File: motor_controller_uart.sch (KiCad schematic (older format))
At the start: 42 parts, among them J10 DB9_Male, J11 DB9_Male, J8 DB9_Male, J9 DB9_Male, U2 MAX3232, U4 MAX3232

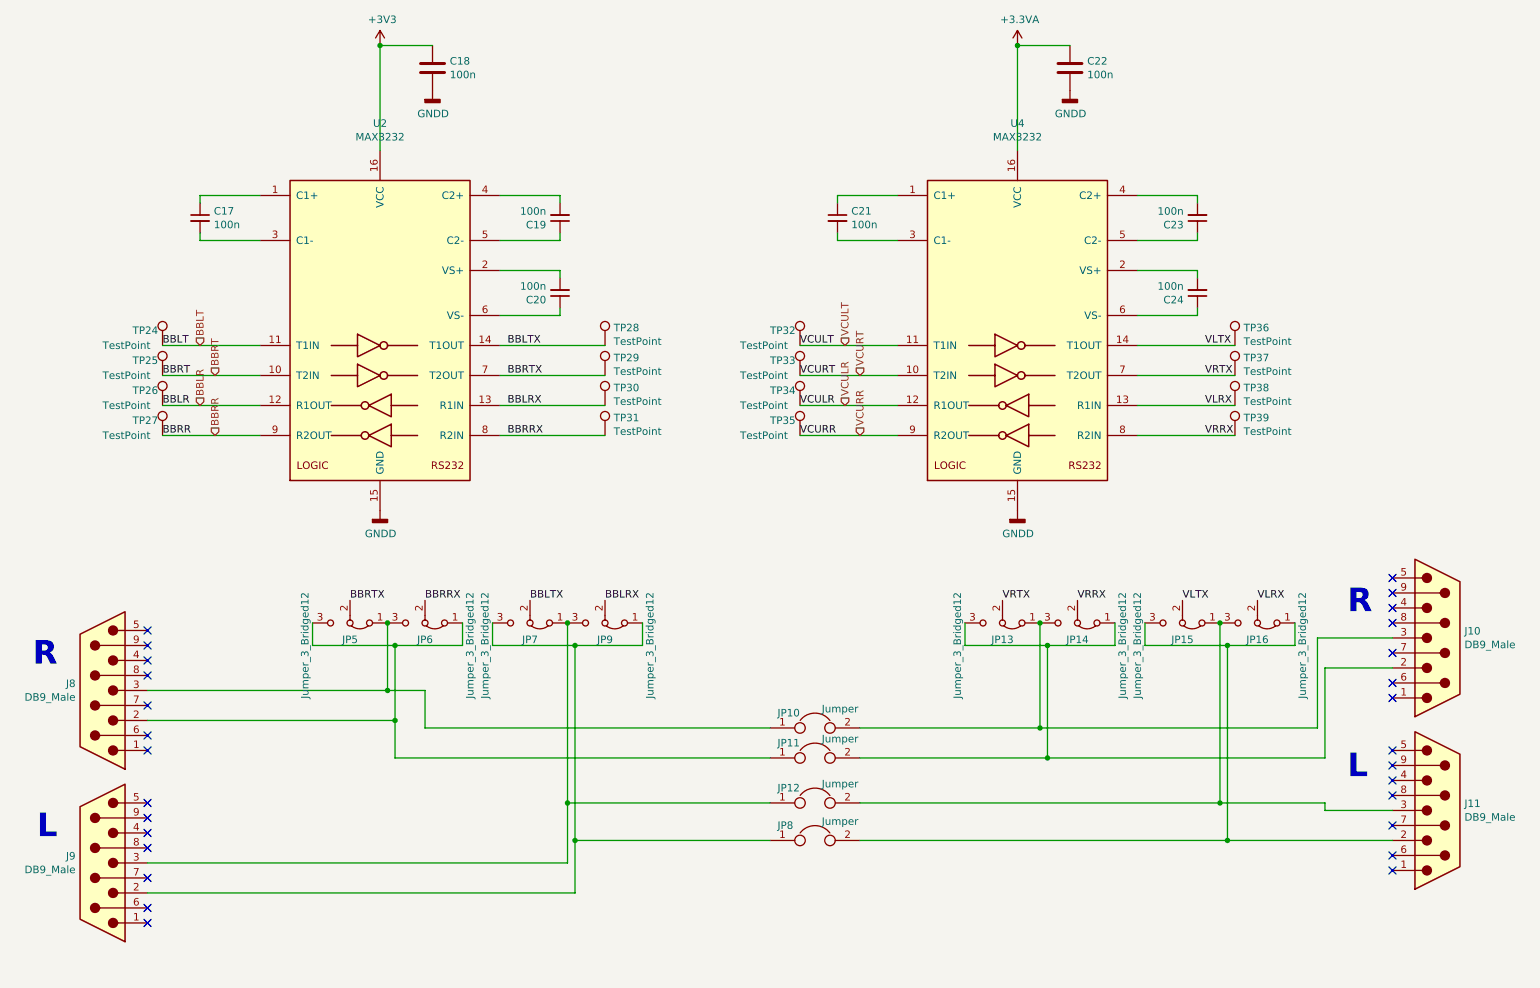
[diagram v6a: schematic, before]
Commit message: rs232/can fix
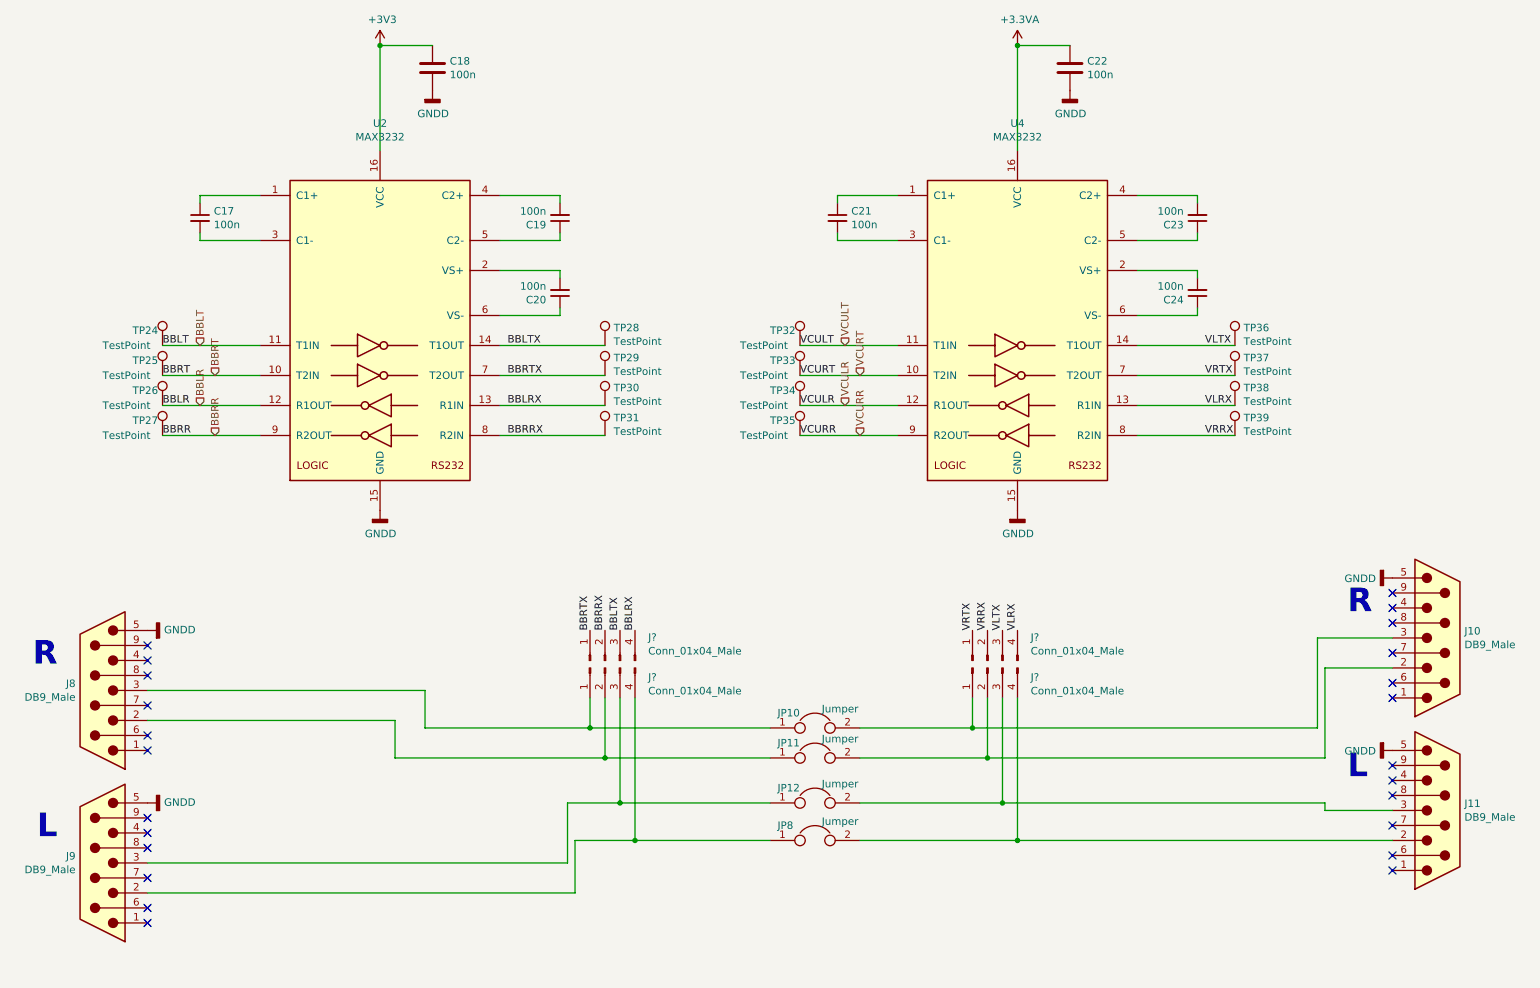
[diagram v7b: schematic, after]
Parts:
- removed JP13, JP14, JP15, JP16, JP5, JP6, JP7, JP9: Jumper_3_Bridged12, Connector_PinHeader_2.00mm:PinHeader_1x03_P2.00mm_Vertical, symbol Jumper:Jumper_3_Bridged12
- added J? (x4): Conn_01x04_Male, symbol Connector:Conn_01x04_Male
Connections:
- net BBLRX: now also J?.4 (Pin_4)
- net BBLTX: now also J?.3 (Pin_3)
- net BBRRX: now also J?.2 (Pin_2)
- net BBRTX: now also J?.1 (Pin_1)
- net GNDD: now also J10.5, J11.5, J8.5, J9.5
- net VLRX: now also J?.4 (Pin_4)
- net VLTX: now also J?.3 (Pin_3)
- net VRRX: now also J?.2 (Pin_2)
- net VRTX: now also J?.1 (Pin_1)
- net at J9.3, JP12.1: now also J?.3 (Pin_3)
- net at J9.2, JP8.1: now also J?.4 (Pin_4)
- net at J8.3, JP10.1: now also J?.1 (Pin_1)
- net at J8.2, JP11.1: now also J?.2 (Pin_2)
- net at J11.3, JP12.2: now also J?.3 (Pin_3)
- net at J11.2, JP8.2: now also J?.4 (Pin_4)
- net at J10.3, JP10.2: now also J?.1 (Pin_1)
- net at J10.2, JP11.2: now also J?.2 (Pin_2)
- no-connect marks 28 -> 24

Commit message: rs232 fix
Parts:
- removed J? (x4): Conn_01x04_Male, symbol Connector:Conn_01x04_Male
- added JP13, JP14, JP15, JP16, JP5, JP6, JP7, JP9: Jumper_3_Bridged12, Connector_PinHeader_2.00mm:PinHeader_1x03_P2.00mm_Vertical, symbol Jumper:Jumper_3_Bridged12
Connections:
- net BBLRX: now also JP8.1, JP9.2 (C)
- net BBLTX: now also JP12.1, JP7.2 (C)
- net BBRRX: now also JP11.1, JP6.2 (C)
- net BBRTX: now also JP10.1, JP5.2 (C)
- net VLRX: now also JP12.2, JP16.2 (C)
- net VLTX: now also JP8.2, JP15.2 (C)
- net VRRX: now also JP10.2, JP14.2 (C)
- net VRTX: now also JP11.2, JP13.2 (C)
- net at J9.3: now also JP7.1 (A), JP9.3 (B); no longer JP12.1
- net at J11.3: now also JP15.1 (A), JP16.3 (B); no longer JP12.2
- net at J8.2: now also JP5.3 (B), JP6.1 (A); no longer JP11.1
- net at J10.2: now also JP13.3 (B), JP14.1 (A); no longer JP11.2
- net at J8.3: now also JP5.1 (A), JP6.3 (B); no longer JP10.1
- net at J10.3: now also JP13.1 (A), JP14.3 (B); no longer JP10.2
- net at J9.2: now also JP7.3 (B), JP9.1 (A); no longer JP8.1
- net at J11.2: now also JP15.3 (B), JP16.1 (A); no longer JP8.2
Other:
- moved on the sheet: J10, J11, J8, J9, JP10, JP11, JP12, JP8
